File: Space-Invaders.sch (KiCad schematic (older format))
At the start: 3 parts

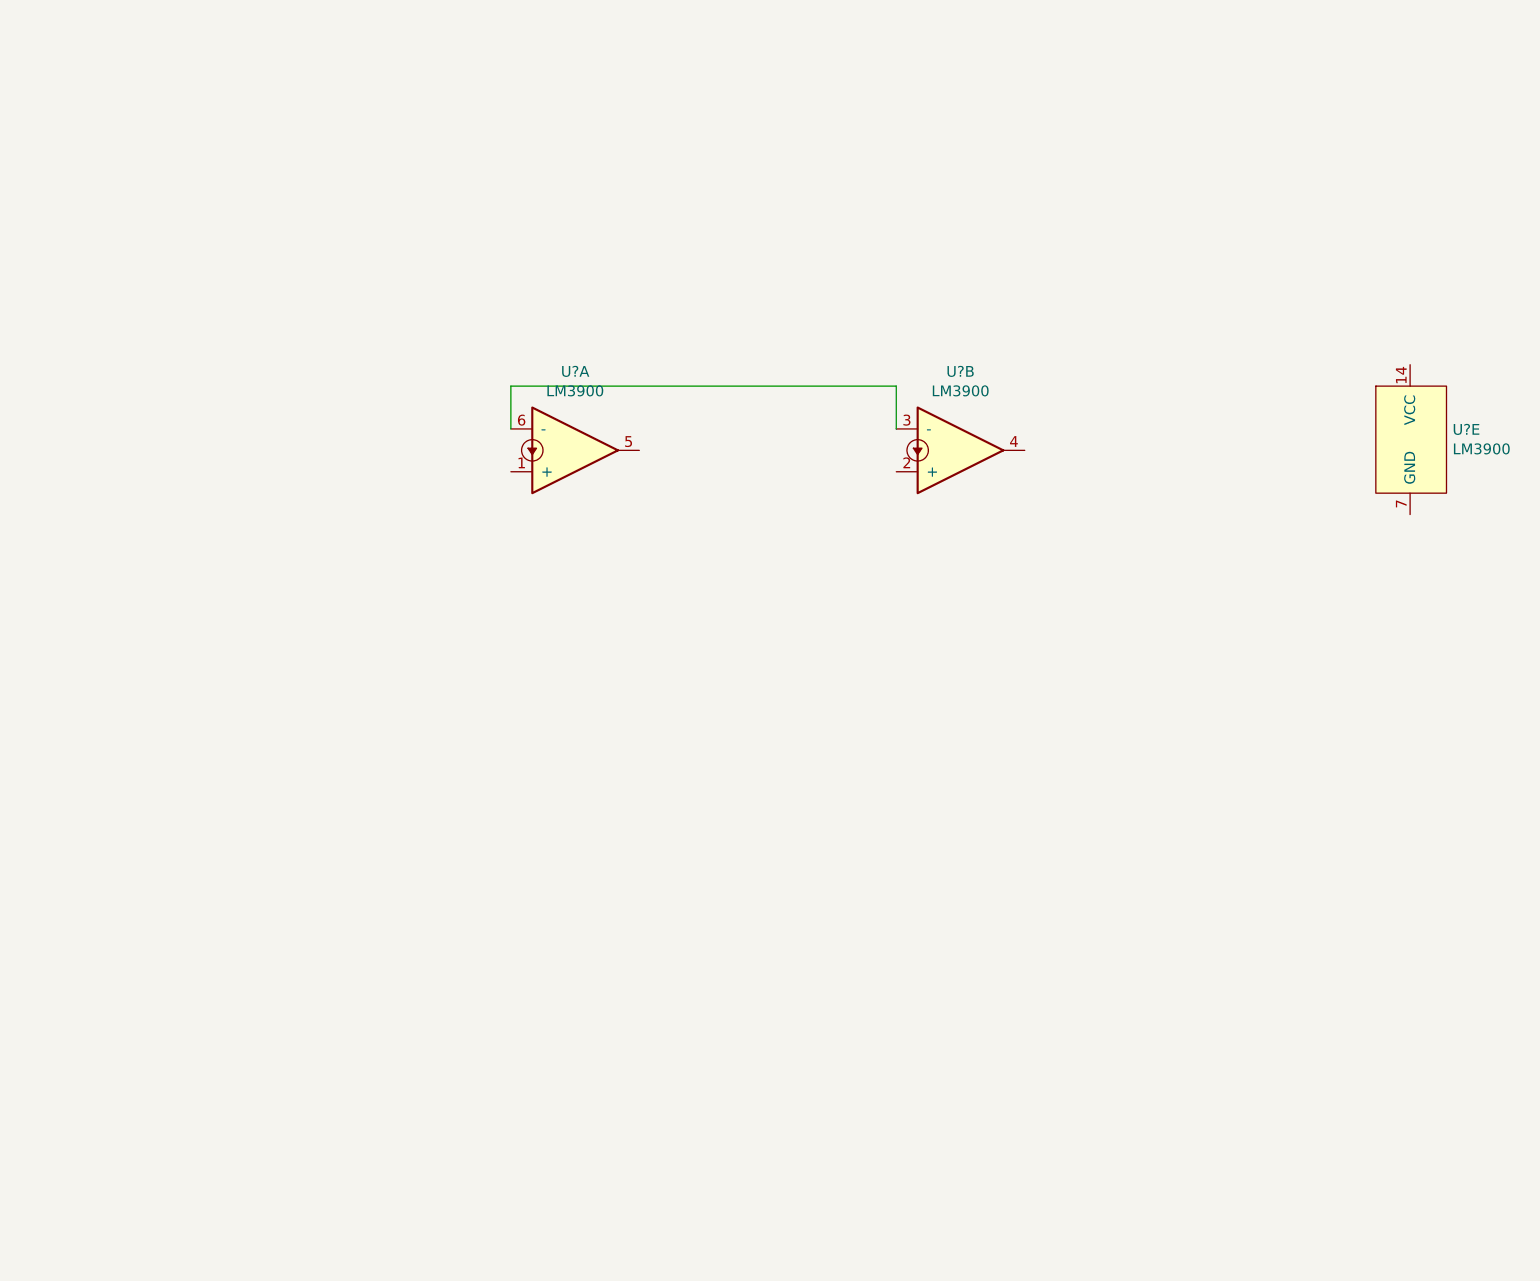
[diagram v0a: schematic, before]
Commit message: added 556
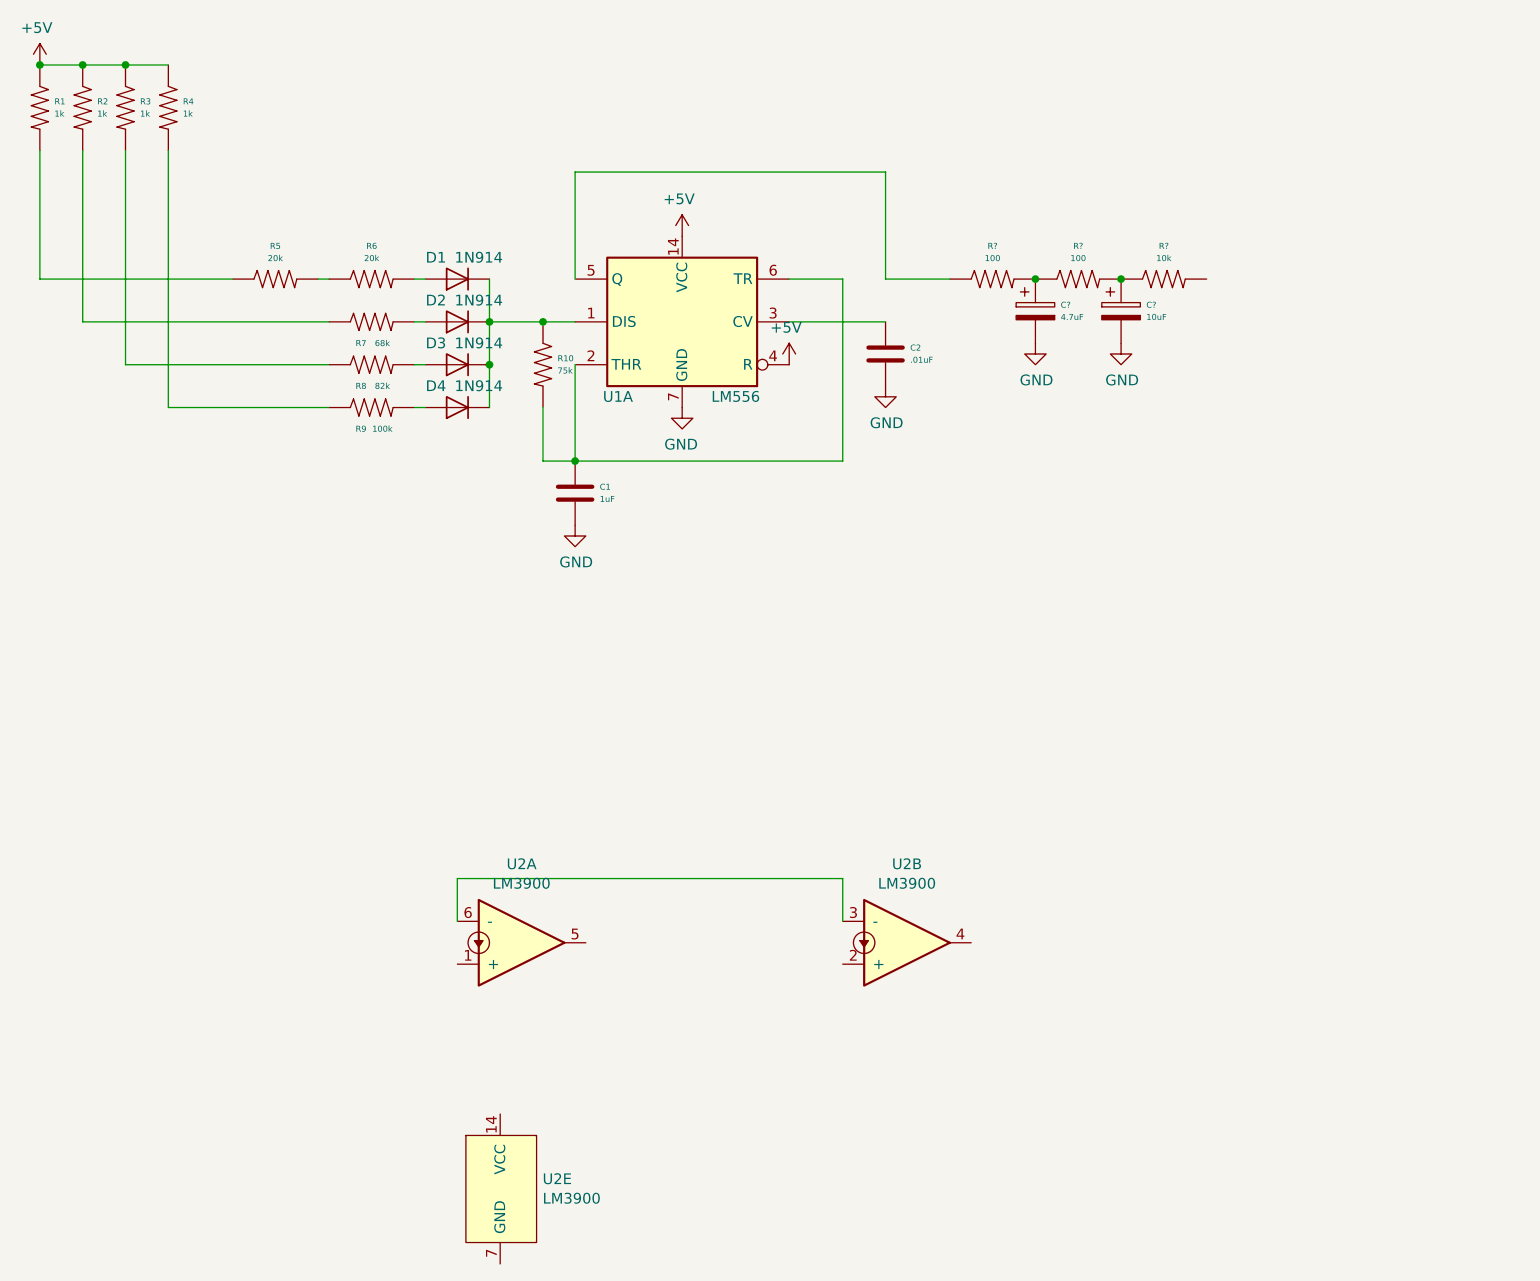
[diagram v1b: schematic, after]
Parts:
- added C1: 1uF, symbol Xenir:Capacitor
- added C2: .01uF, symbol Xenir:Capacitor
- added C?: 4.7uF, symbol Xenir:Cap_Polarized
- added C?: 10uF, symbol Xenir:Cap_Polarized
- added D1, D2, D3, D4: 1N914, Diode_THT:D_DO-35_SOD27_P7.62mm_Horizontal, symbol Diode:1N914
- added R1, R2, R3, R4: 1k, symbol Xenir:Resistor
- added R10: 75k, symbol Xenir:Resistor
- added R5, R6: 20k, symbol Xenir:Resistor
- added R7: 68k, symbol Xenir:Resistor
- added R8: 82k, symbol Xenir:Resistor
- added R9: 100k, symbol Xenir:Resistor
- added R? (x2): 100, symbol Xenir:Resistor
- added R?: 10k, symbol Xenir:Resistor
- added U1: LM556, symbol Timer:LM556
- gave numbers to parts that had none: 1
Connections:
- new net: D1.1 (K), D2.1 (K), D3.1 (K), D4.1 (K), R10.1, U1.1 (DIS)
- new net: C1.1, R10.2, U1.2 (THR), U1.6 (TR)
- new net: C2.1, U1.3 (CV)
- new net: R?.1, U1.5 (Q)
- new net: R1.2, R5.1
- new net: R5.2, R6.1
- new net: D1.2 (A), R6.2
- new net: R2.2, R7.1
- new net: D2.2 (A), R7.2
- new net: R3.2, R8.1
- new net: D3.2 (A), R8.2
- new net: R4.2, R9.1
- new net: D4.2 (A), R9.2
- new net: C?.1, R?.1, R?.2 (x2)
- new net +5V: R1.1, R2.1, R3.1, R4.1, U1.14 (VCC), U1.4 (R)
- new net GND: C1.2, C2.2, C?.2, C?.2, U1.7 (GND)
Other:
- moved on the sheet: U2A, U2B, U2E

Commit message: added steps
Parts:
- removed R1, R2, R3, R4: 1k, symbol Xenir:Resistor
- added Q? (x4): BS170, Package_TO_SOT_THT:TO-92_Inline, symbol Transistor_FET:BS170
- added R? (x8): 1k, symbol Xenir:Resistor
- added R? (x4): 10k, symbol Xenir:Resistor
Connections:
- net +5V: now also R?.2, R?.2, R?.2, R?.2
- net GND: now also Q?.3 (S), Q?.3 (S), Q?.3 (S), Q?.3 (S), R?.1, R?.1, R?.1, R?.1
- net SW1: now reaches R5.1
- net SW1: now also Q?.1 (D), R?.1
- net SW2: now reaches R7.1
- net SW2: now also Q?.1 (D), R?.1
- net SW3: now reaches R8.1
- net SW3: now also Q?.1 (D), R?.1
- net SW4: now reaches R9.1
- net SW4: now also Q?.1 (D), R?.1
- net OUTPUT: now reaches R?.2
- new net: Q?.2 (G), R?.1, R?.2 (x4)
- new net GPIO1: R?.2
- new net GPIO2: R?.2
- new net GPIO3: R?.2
- new net GPIO4: R?.2
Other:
- note added: "INVADER STEPS"
- moved on the sheet: C1, C2, C?, D1, D2, D3, D4, R10, R5, R6, R7, R8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

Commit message: added noise
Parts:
- added C?: 1nF, symbol Xenir:Capacitor
- added R? (x3): 56k, symbol Xenir:Resistor
- added R?: 560k, symbol Xenir:Resistor
- added U? (x3): 4070, symbol 4xxx:4070
- added U?: 4006, symbol 4xxx_IEEE:4006
- added U?: CD4006, symbol Xenir:CD4006
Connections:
- net labels added: +12V, NOISE
- wire segments 35 -> 66
- no-connect marks 0 -> 2
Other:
- note added: "NOISE\nGENERATOR"
- moved on the sheet: C1, C2, C?, D1, D2, D3, D4, Q?, R10, R5, R6, R7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

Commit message: added killed
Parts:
- removed U?: 4006, symbol 4xxx_IEEE:4006
- added C10, C9: .1uF, symbol Xenir:Capacitor
- added C6: 470p, symbol Xenir:Capacitor
- added C7: 2.2uF, symbol Xenir:Capacitor
- added C8: 1uF, symbol Xenir:Capacitor
- added D5, D6: 1N914, Diode_THT:D_DO-35_SOD27_P7.62mm_Horizontal, symbol Diode:1N914
- added R26: 1k, symbol Xenir:Resistor
- added R27, R31: 1M, symbol Xenir:Resistor
- added R28: 100k, symbol Xenir:Resistor
- added R29: 4.7M, symbol Xenir:Resistor
- added R30: 2.2M, symbol Xenir:Resistor
- added R32: 10k, symbol Xenir:Resistor
- added R33, R34, R36: 680k, symbol Xenir:Resistor
- added R35: 2.7M, symbol Xenir:Resistor
- added R37: 27k, symbol Xenir:Resistor
- added R38: 560, symbol Xenir:Resistor
- added R39: 6.8k, symbol Xenir:Resistor
- added R40: 2k, symbol Xenir:Resistor
- R19: renamed from R?; value 56k -> 27k
- R22: renamed from R?; value 56k -> 270k
- gave numbers to parts that had none: 26
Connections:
- wire segments 66 -> 98
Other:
- note added: "PLAYER\nKILLED"
- moved on the sheet: U2A, U2E

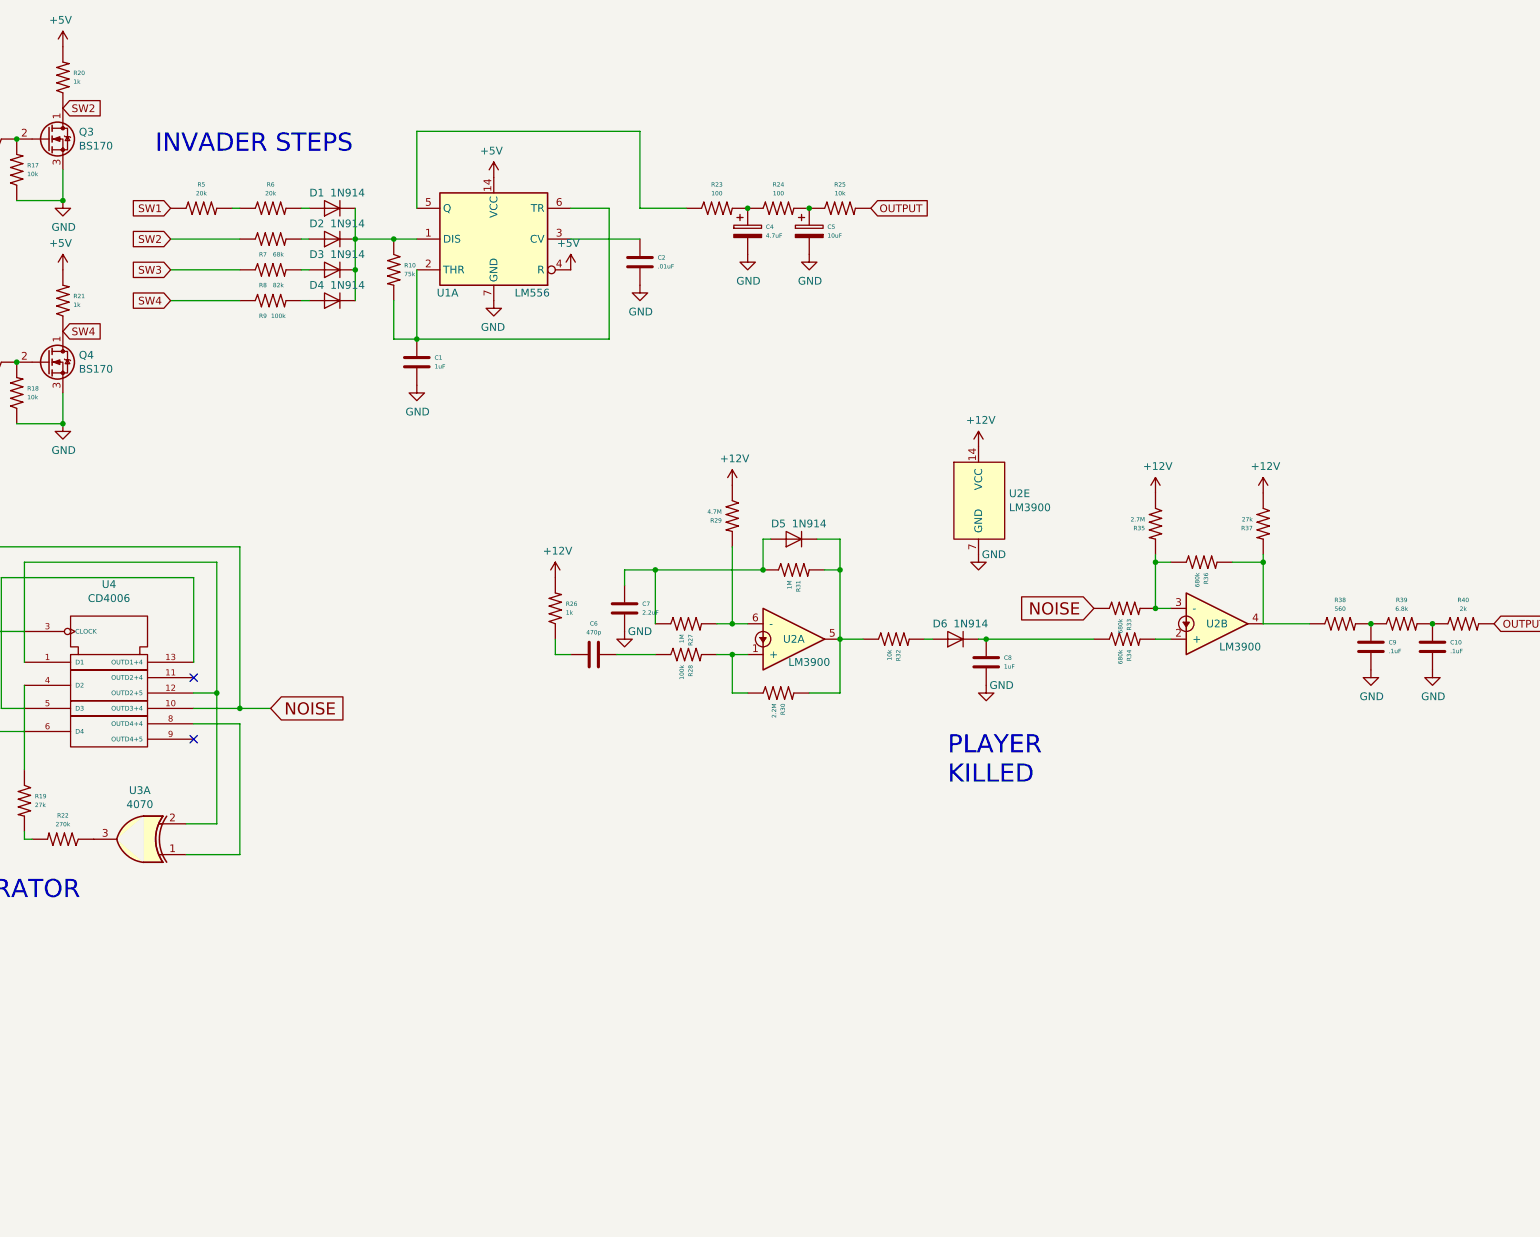
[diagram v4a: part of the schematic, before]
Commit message: added output
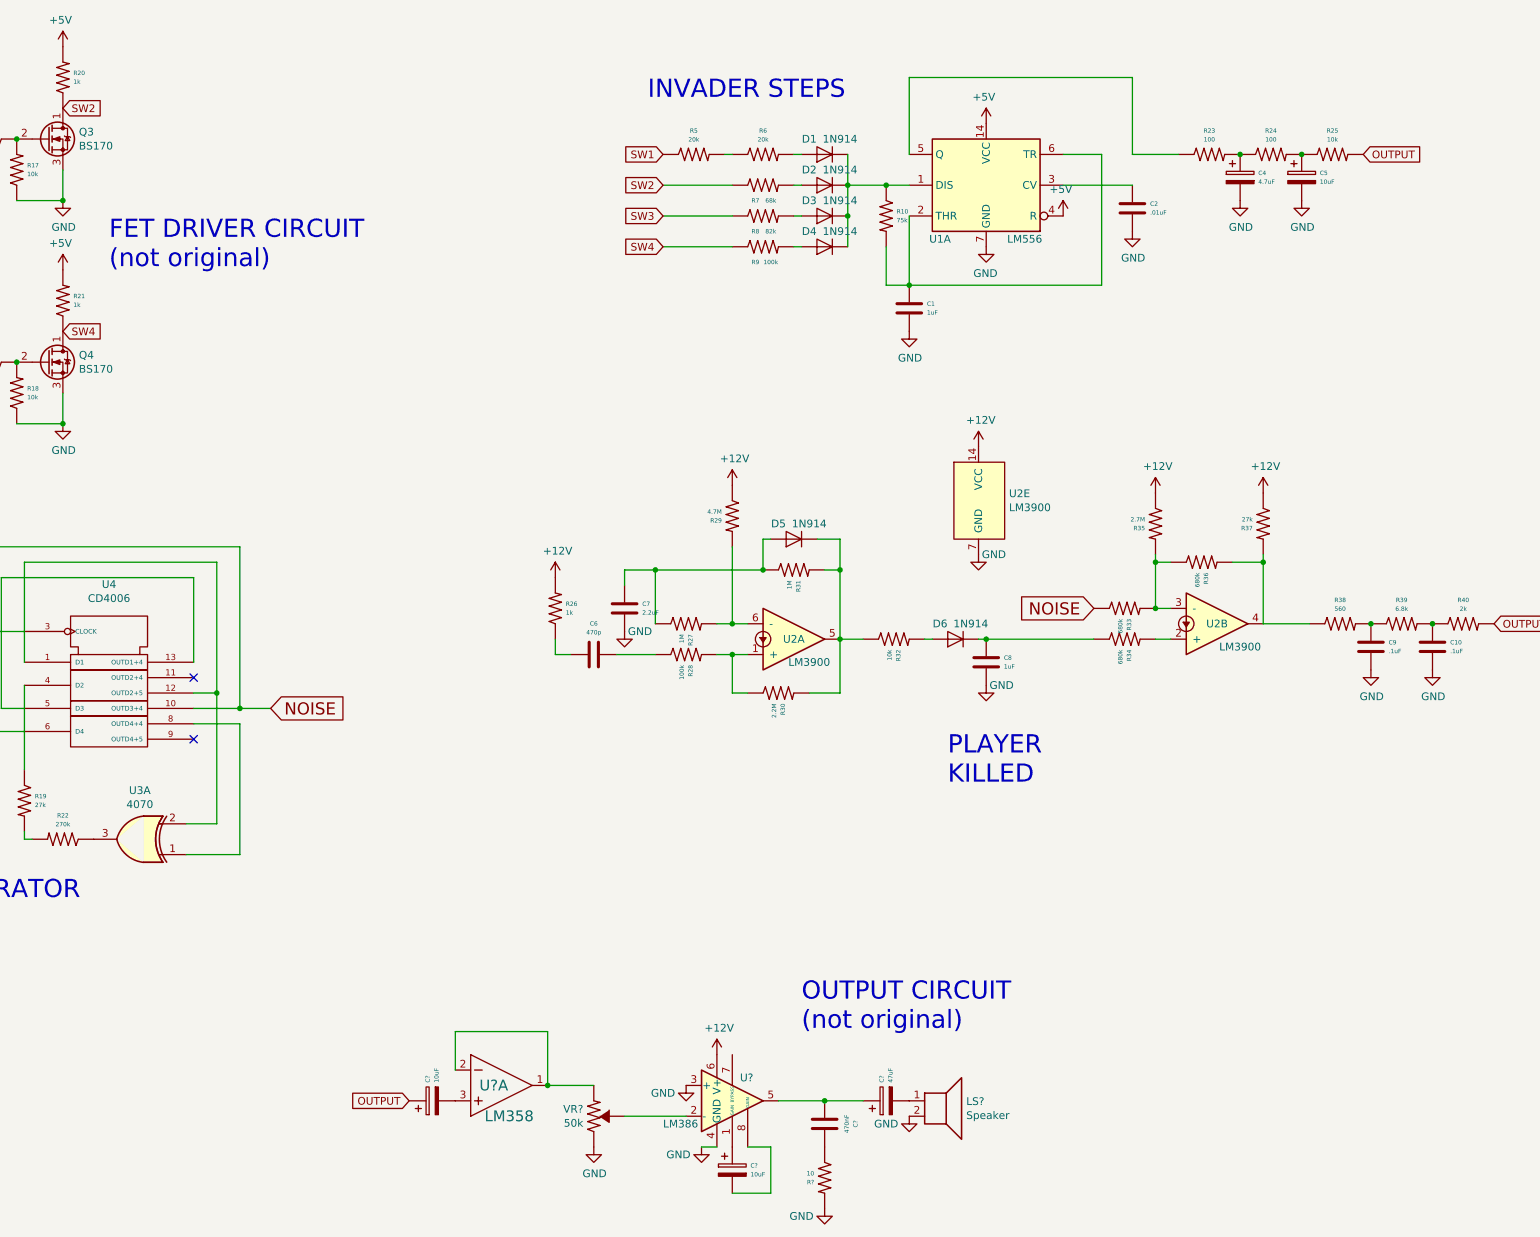
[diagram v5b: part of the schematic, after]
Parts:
- added C? (x2): 10uF, symbol Xenir:Cap_Polarized
- added C?: 470nF, symbol Xenir:Capacitor
- added C?: 47uF, symbol Xenir:Cap_Polarized
- added LS?: Speaker, symbol Device:Speaker
- added R?: 10, symbol Xenir:Resistor
- added U?: LM358, symbol Xenir:LM358
- added U?: LM386, symbol Amplifier_Audio:LM386
- added VR?: 50k, symbol Xenir:Trimpot
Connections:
- net +12V: now also U?.6 (V+)
- net GND: now also LS?.2, R?.2, U?.3 (+), U?.4 (GND), VR?.1 (CW)
- net OUTPUT: now also C?.1
- new net: U?.1 (OUT), U?.2 (-IN), VR?.3 (CCW)
- new net: C?.2, U?.3 (+IN)
- new net: C?.1, U?.1 (GAIN)
- new net: U?.2 (-), VR?.2 (WIPER)
- new net: C?.1, C?.1, U?.5
- new net: C?.2, U?.8 (GAIN)
- new net: C?.2, R?.1
- new net: C?.2, LS?.1
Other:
- note added: "FET DRIVER CIRCUIT\n(not original)"
- note added: "OUTPUT CIRCUIT\n(not original)"
- moved on the sheet: C1, C2, C4, C5, D1, D2, D3, D4, R10, R23, R24, R25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
